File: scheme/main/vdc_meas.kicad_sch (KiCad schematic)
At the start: 22 parts, among them U12 AMC1311, U13 RS8551

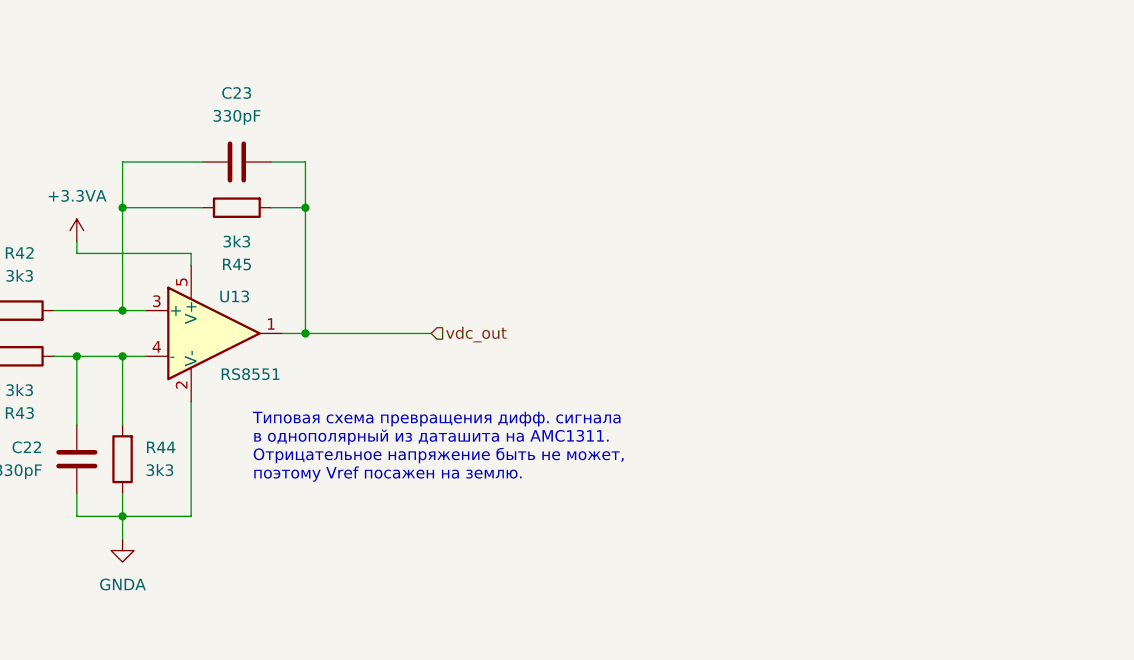
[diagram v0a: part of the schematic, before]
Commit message: added decoupling capacitors
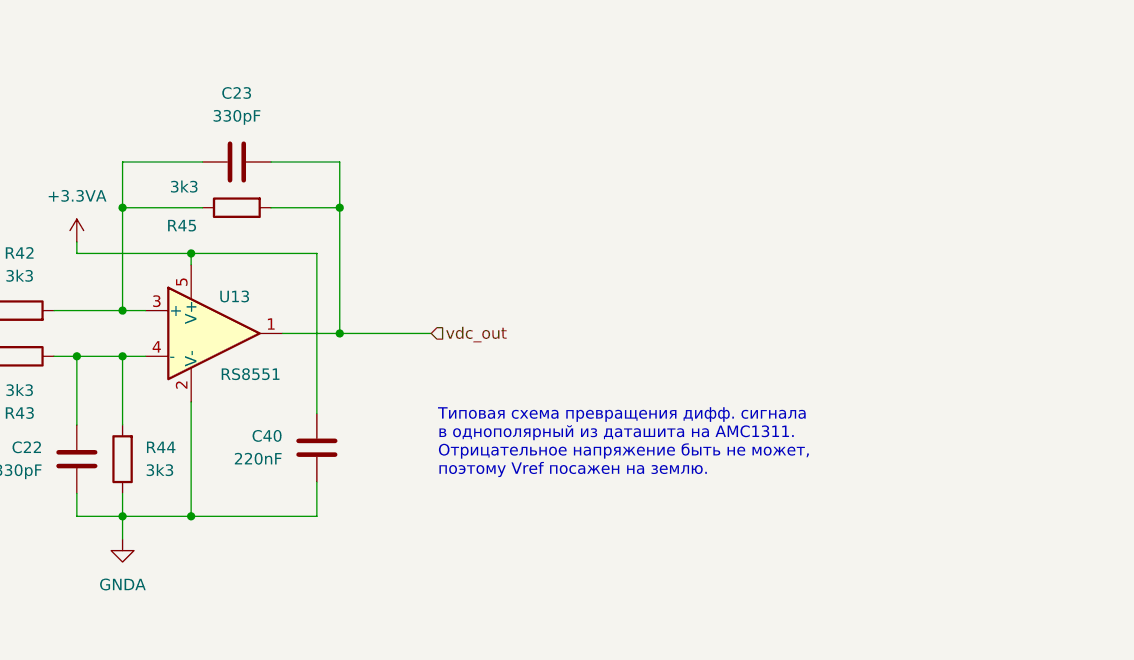
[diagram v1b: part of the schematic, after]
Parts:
- added C40: 220nF, Capacitor_SMD:C_0805_2012Metric, symbol Device:C
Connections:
- net +3.3VA: now also C40.1
- net GNDA: now also C40.2
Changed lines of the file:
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@@
+	)
+	(junction
+		(at 215.9 80.01)
+		(diameter 0)
+		(color 0 0 0 0)
 	)
 	(junction
@@
 	)
 	(junction
-		(at 212.09 80.01)
-		(diameter 0)
-		(color 0 0 0 0)
-	)
-	(junction
 		(at 186.69 82.55)
 		(diameter 0)
@@
 	)
 	(junction
+		(at 199.39 100.33)
+		(diameter 0)
+		(color 0 0 0 0)
+	)
+	(junction
 		(at 138.43 68.58)
 		(diameter 0)
@@
 	)
 	(junction
+		(at 199.39 71.12)
+		(diameter 0)
+		(color 0 0 0 0)
+	)
+	(junction
 		(at 191.77 66.04)
 		(diameter 0)
@@
 	)
 	(junction
+		(at 215.9 66.04)
+		(diameter 0)
+		(color 0 0 0 0)
+	)
+	(junction
 		(at 102.87 68.58)
 		(diameter 0)
@@
 		(color 0 0 0 0)
 	)
-	(junction
-		(at 212.09 66.04)
-		(diameter 0)
-		(color 0 0 0 0)
-	)
 	(wire
 		(pts
@@
 	(wire
 		(pts
-			(xy 212.09 66.04) (xy 212.09 80.01)
+			(xy 215.9 66.04) (xy 215.9 80.01)
 		)
 		(stroke
@@
 	(wire
 		(pts
+			(xy 213.36 71.12) (xy 199.39 71.12)
+		)
+		(stroke
+			(width 0)
+			(type default)
+		)
+	)
+	(wire
+		(pts
 			(xy 152.4 68.58) (xy 138.43 68.58)
 		)
@@
 	(wire
 		(pts
+			(xy 213.36 100.33) (xy 199.39 100.33)
+		)
+		(stroke
+			(width 0)
+			(type default)
+		)
+	)
+	(wire
+		(pts
 			(xy 191.77 66.04) (xy 191.77 77.47)
 		)
@@
 	(wire
 		(pts
-			(xy 208.28 66.04) (xy 212.09 66.04)
+			(xy 208.28 66.04) (xy 215.9 66.04)
 		)
 		(stroke
@@
 	(wire
 		(pts
+			(xy 213.36 88.9) (xy 213.36 71.12)
+		)
+		(stroke
+			(width 0)
+			(type default)
+		)
+	)
+	(wire
+		(pts
 			(xy 63.5 76.2) (xy 59.69 76.2)
 		)
@@
 	(wire
 		(pts
-			(xy 209.55 80.01) (xy 212.09 80.01)
+			(xy 209.55 80.01) (xy 215.9 80.01)
 		)
 		(stroke
@@
 	(wire
 		(pts
+			(xy 213.36 96.52) (xy 213.36 100.33)
+		)
+		(stroke
+			(width 0)
+			(type default)
+		)
+	)
+	(wire
+		(pts
 			(xy 184.15 77.47) (xy 191.77 77.47)
 		)
@@
 	(wire
 		(pts
+			(xy 215.9 80.01) (xy 226.06 80.01)
+		)
+		(stroke
+			(width 0)
+			(type default)
+		)
+	)
+	(wire
+		(pts
 			(xy 186.69 82.55) (xy 191.77 82.55)
 		)
@@
 	(wire
 		(pts
-			(xy 212.09 80.01) (xy 226.06 80.01)
-		)
-		(stroke
-			(width 0)
-			(type default)
-		)
-	)
-	(wire
-		(pts
 			(xy 133.35 67.31) (xy 133.35 68.58)
 		)
@@
 	(wire
 		(pts
-			(xy 208.28 60.96) (xy 212.09 60.96)
+			(xy 208.28 60.96) (xy 215.9 60.96)
 		)
 		(stroke
@@
 	(wire
 		(pts
-			(xy 212.09 60.96) (xy 212.09 66.04)
+			(xy 215.9 60.96) (xy 215.9 66.04)
 		)
 		(stroke
@@
 	(text "Типовая схема превращения дифф. сигнала\nв однополярный из даташита на AMC1311.\nОтрицательное напряжение быть не может,\nпоэтому Vref посажен на землю."
 		(exclude_from_sim no)
-		(at 206.248 92.71 0)
+		(at 226.822 92.202 0)
 		(effects
 			(font
@@
 		(dnp no)
 		(property "Reference" "R45"
-			(at 204.47 72.39 90)
+			(at 198.374 68.072 90)
 			(effects
 				(font
@@
 		)
 		(property "Value" "3k3"
-			(at 204.47 69.85 90)
+			(at 198.628 63.754 90)
 			(effects
 				(font
@@
 					(unit 1)
 				)
+			)
+		)
+	)
+	(symbol
+		(lib_id "Device:C")
+		(at 213.36 92.71 0)
+		(mirror y)
+		(unit 1)
+		(exclude_from_sim no)
+		(in_bom yes)
+		(on_board yes)
+		(dnp no)
+		(property "Reference" "C40"
+			(at 209.55 91.4399 0)
+			(effects
+				(font
+					(size 1.27 1.27)
+				)
+				(justify left)
+			)
+		)
+		(property "Value" "220nF"
+			(at 209.55 93.9799 0)
+			(effects
+				(font
+					(size 1.27 1.27)
+				)
+				(justify left)
+			)
+		)
+		(property "Footprint" "Capacitor_SMD:C_0805_2012Metric"
+			(at 212.3948 96.52 0)
+			(effects
+				(font
+					(size 1.27 1.27)
+				)
+				(hide yes)
+			)
+		)
+		(property "Datasheet" "~"
+			(at 213.36 92.71 0)
+			(effects
+				(font
+					(size 1.27 1.27)
+				)
+				(hide yes)
+			)
+		)
+		(property "Description" "Unpolarized capacitor"
+			(at 213.36 92.71 0)
+			(effects
+				(font
+					(size 1.27 1.27)
+				)
+				(hide yes)
+			)
+		)
+		(pin "2"
+		)
+		(pin "1"
+		)
+		(instances
+			(project "main"
+				(path "/c11d1dbc-4db9-4712-8d1d-5f6f7086cded/5d407613-ca47-4478-86ea-137e1786be86/ac75aa1d-a28e-4560-8180-07db9e006832"
+					(reference "C40")
+					(unit 1)
+				)

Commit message: bootstrap dc-dc add capacitors & more
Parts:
- renumbered C26 to C21, C27 to C22, C21 to C23, C29 to C26, C28 to C27, C22 to C28, C23 to C29, R51 to R40, R48 to R41, R49 to R42, R50 to R43, R52 to R44, R47 to R45, R40 to R47, R41 to R48, R42 to R49, R43 to R50, R44 to R51, R45 to R52

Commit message: separate hi power & signal gnd
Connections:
- net GNDPWR renamed GNDH
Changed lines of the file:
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@@
-	)
-	(symbol
-		(lib_id "power:GNDPWR")
-		(at 67.31 90.17 0)
-		(unit 1)
-		(exclude_from_sim no)
-		(in_bom yes)
-		(on_board yes)
-		(dnp no)
-		(property "Reference" "#PWR29"
-			(at 67.31 95.25 0)
-			(effects
-				(font
-					(size 1.27 1.27)
-				)
-				(hide yes)
-			)
-		)
-		(property "Value" "GNDPWR"
-			(at 67.183 93.98 0)
-			(effects
-				(font
-					(size 1.27 1.27)
-				)
-			)
-		)
-		(property "Footprint" ""
-			(at 67.31 91.44 0)
-			(effects
-				(font
-					(size 1.27 1.27)
-				)
-				(hide yes)
-			)
-		)
-		(property "Datasheet" ""
-			(at 67.31 91.44 0)
-			(effects
-				(font
-					(size 1.27 1.27)
-				)
-				(hide yes)
-			)
-		)
-		(property "Description" "Power symbol creates a global label with name \"GNDPWR\" , global ground"
-			(at 67.31 90.17 0)
-			(effects
-				(font
-					(size 1.27 1.27)
-				)
-				(hide yes)
-			)
-		)
-		(pin "1"
-		)
-		(instances
-			(project "main"
-				(path "/c11d1dbc-4db9-4712-8d1d-5f6f7086cded/65f1abf4-f16e-41b7-92a2-6e9eb3d99d97"
-					(reference "#PWR29")
-					(unit 1)
-				)
-			)
-		)
 	)
 	(symbol
@@
 	)
 	(symbol
-		(lib_id "power:GNDPWR")
-		(at 123.19 95.25 0)
-		(unit 1)
-		(exclude_from_sim no)
-		(in_bom yes)
-		(on_board yes)
-		(dnp no)
-		(property "Reference" "#PWR30"
-			(at 123.19 100.33 0)
-			(effects
-				(font
-					(size 1.27 1.27)
-				)
-				(hide yes)
-			)
-		)
-		(property "Value" "GNDPWR"
-			(at 123.063 99.06 0)
-			(effects
-				(font
-					(size 1.27 1.27)
-				)
-			)
-		)
-		(property "Footprint" ""
-			(at 123.19 96.52 0)
-			(effects
-				(font
-					(size 1.27 1.27)
-				)
-				(hide yes)
-			)
-		)
-		(property "Datasheet" ""
-			(at 123.19 96.52 0)
-			(effects
-				(font
-					(size 1.27 1.27)
-				)
-				(hide yes)
-			)
-		)
-		(property "Description" "Power symbol creates a global label with name \"GNDPWR\" , global ground"
-			(at 123.19 95.25 0)
-			(effects
-				(font
-					(size 1.27 1.27)
-				)
-				(hide yes)
-			)
-		)
-		(pin "1"
-		)
-		(instances
-			(project "main"
-				(path "/c11d1dbc-4db9-4712-8d1d-5f6f7086cded/65f1abf4-f16e-41b7-92a2-6e9eb3d99d97"
-					(reference "#PWR30")
-					(unit 1)
-				)
-			)
-		)
-	)
-	(symbol
 		(lib_id "Device:C")
 		(at 204.47 60.96 270)
@@
 					(unit 1)
 				)
+			)
+		)
+	)
+	(symbol
+		(lib_id "main:GNDH")
+		(at 67.31 90.17 0)
+		(unit 1)
+		(exclude_from_sim no)
+		(in_bom yes)
+		(on_board yes)
+		(dnp no)
+		(fields_autoplaced yes)
+		(property "Reference" "#PWR029"
+			(at 67.31 96.52 0)
+			(effects
+				(font
+					(size 1.27 1.27)
+				)
+				(hide yes)
+			)
+		)
+		(property "Value" "GNDH"
+			(at 67.31 95.25 0)
+			(effects
+				(font
+					(size 1.27 1.27)
+				)
+			)
+		)
+		(property "Footprint" ""
+			(at 67.31 90.17 0)
+			(effects
+				(font
+					(size 1.27 1.27)
+				)
+				(hide yes)
+			)
+		)
+		(property "Datasheet" ""
+			(at 67.31 90.17 0)
+			(effects
+				(font
+					(size 1.27 1.27)
+				)
+				(hide yes)
+			)
+		)
+		(property "Description" "Power symbol creates a global label with name \"GNDH\" , hi ground"
+			(at 67.31 90.17 0)
+			(effects
+				(font
+					(size 1.27 1.27)
+				)
+				(hide yes)
+			)
+		)
+		(pin "1"
+		)
+		(instances
+			(project "main"
+				(path "/c11d1dbc-4db9-4712-8d1d-5f6f7086cded/65f1abf4-f16e-41b7-92a2-6e9eb3d99d97"
+					(reference "#PWR029")
+					(unit 1)
+				)
+			)
+		)
+	)
+	(symbol
+		(lib_id "main:GNDH")
+		(at 123.19 95.25 0)
+		(unit 1)
+		(exclude_from_sim no)
+		(in_bom yes)
+		(on_board yes)
+		(dnp no)
+		(fields_autoplaced yes)
+		(property "Reference" "#PWR030"
+			(at 123.19 101.6 0)
+			(effects
+				(font
+					(size 1.27 1.27)
+				)
+				(hide yes)
+			)
+		)
+		(property "Value" "GNDH"
+			(at 123.19 100.33 0)
+			(effects
+				(font
+					(size 1.27 1.27)
+				)
+			)
+		)
+		(property "Footprint" ""
+			(at 123.19 95.25 0)
+			(effects
+				(font
+					(size 1.27 1.27)
+				)
+				(hide yes)
+			)
+		)
+		(property "Datasheet" ""
+			(at 123.19 95.25 0)
+			(effects
+				(font
+					(size 1.27 1.27)
+				)
+				(hide yes)
+			)
+		)
+		(property "Description" "Power symbol creates a global label with name \"GNDH\" , hi ground"
+			(at 123.19 95.25 0)
+			(effects
+				(font
+					(size 1.27 1.27)
+				)
+				(hide yes)
+			)
+		)
+		(pin "1"
+		)
+		(instances
+			(project "main"
+				(path "/c11d1dbc-4db9-4712-8d1d-5f6f7086cded/65f1abf4-f16e-41b7-92a2-6e9eb3d99d97"
+					(reference "#PWR030")
+					(unit 1)
+				)

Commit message: boards schematic sheets & more
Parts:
- added R107: 22R, Resistor_SMD:R_0805_2012Metric, symbol Device:R
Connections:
- net vdc_out: now also R107.2; no longer C29.1, R52.2, U13.1
- new net: C29.1, R107.1, R52.2, U13.1
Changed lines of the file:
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@@
+	)
+	(junction
+		(at 116.84 77.47)
+		(diameter 0)
+		(color 0 0 0 0)
+	)
+	(junction
+		(at 102.87 92.71)
+		(diameter 0)
+		(color 0 0 0 0)
+	)
+	(junction
+		(at 186.69 82.55)
+		(diameter 0)
+		(color 0 0 0 0)
+	)
+	(junction
+		(at 152.4 92.71)
+		(diameter 0)
+		(color 0 0 0 0)
+	)
+	(junction
+		(at 199.39 100.33)
+		(diameter 0)
+		(color 0 0 0 0)
+	)
+	(junction
+		(at 138.43 68.58)
+		(diameter 0)
+		(color 0 0 0 0)
+	)
+	(junction
+		(at 133.35 68.58)
+		(diameter 0)
+		(color 0 0 0 0)
+	)
+	(junction
+		(at 191.77 82.55)
+		(diameter 0)
+		(color 0 0 0 0)
+	)
+	(junction
+		(at 138.43 92.71)
+		(diameter 0)
+		(color 0 0 0 0)
+	)
+	(junction
+		(at 199.39 71.12)
+		(diameter 0)
+		(color 0 0 0 0)
+	)
+	(junction
+		(at 191.77 66.04)
+		(diameter 0)
+		(color 0 0 0 0)
+	)
+	(junction
+		(at 191.77 77.47)
+		(diameter 0)
+		(color 0 0 0 0)
+	)
+	(junction
+		(at 215.9 66.04)
+		(diameter 0)
+		(color 0 0 0 0)
+	)
+	(junction
+		(at 102.87 68.58)
+		(diameter 0)
+		(color 0 0 0 0)
 	)
 	(junction
@@
 	)
 	(junction
-		(at 116.84 77.47)
-		(diameter 0)
-		(color 0 0 0 0)
-	)
-	(junction
-		(at 102.87 92.71)
-		(diameter 0)
-		(color 0 0 0 0)
-	)
-	(junction
-		(at 186.69 82.55)
-		(diameter 0)
-		(color 0 0 0 0)
-	)
-	(junction
-		(at 152.4 92.71)
-		(diameter 0)
-		(color 0 0 0 0)
-	)
-	(junction
-		(at 199.39 100.33)
-		(diameter 0)
-		(color 0 0 0 0)
-	)
-	(junction
-		(at 138.43 68.58)
-		(diameter 0)
-		(color 0 0 0 0)
-	)
-	(junction
-		(at 133.35 68.58)
-		(diameter 0)
-		(color 0 0 0 0)
-	)
-	(junction
-		(at 191.77 82.55)
-		(diameter 0)
-		(color 0 0 0 0)
-	)
-	(junction
-		(at 138.43 92.71)
-		(diameter 0)
-		(color 0 0 0 0)
-	)
-	(junction
-		(at 199.39 71.12)
-		(diameter 0)
-		(color 0 0 0 0)
-	)
-	(junction
-		(at 191.77 66.04)
-		(diameter 0)
-		(color 0 0 0 0)
-	)
-	(junction
-		(at 191.77 77.47)
-		(diameter 0)
-		(color 0 0 0 0)
-	)
-	(junction
-		(at 215.9 66.04)
-		(diameter 0)
-		(color 0 0 0 0)
-	)
-	(junction
-		(at 102.87 68.58)
-		(diameter 0)
-		(color 0 0 0 0)
-	)
-	(junction
 		(at 116.84 92.71)
 		(diameter 0)
@@
 	(wire
 		(pts
+			(xy 215.9 80.01) (xy 219.71 80.01)
+		)
+		(stroke
+			(width 0)
+			(type default)
+		)
+	)
+	(wire
+		(pts
 			(xy 191.77 82.55) (xy 191.77 90.17)
 		)
@@
 	(wire
 		(pts
+			(xy 227.33 80.01) (xy 231.14 80.01)
+		)
+		(stroke
+			(width 0)
+			(type default)
+		)
+	)
+	(wire
+		(pts
 			(xy 63.5 36.83) (xy 67.31 36.83)
 		)
@@
 		(pts
 			(xy 165.1 92.71) (xy 152.4 92.71)
-		)
-		(stroke
-			(width 0)
-			(type default)
-		)
-	)
-	(wire
-		(pts
-			(xy 215.9 80.01) (xy 226.06 80.01)
 		)
 		(stroke
@@
 	(hierarchical_label "vdc_out"
 		(shape output)
-		(at 226.06 80.01 0)
+		(at 231.14 80.01 0)
 		(fields_autoplaced yes)
 		(effects
@@
 					(unit 1)
 				)
+			)
+		)
+	)
+	(symbol
+		(lib_id "Device:R")
+		(at 223.52 80.01 90)
+		(unit 1)
+		(exclude_from_sim no)
+		(in_bom yes)
+		(on_board yes)
+		(dnp no)
+		(fields_autoplaced yes)
+		(property "Reference" "R107"
+			(at 223.52 73.66 90)
+			(effects
+				(font
+					(size 1.27 1.27)
+				)
+			)
+		)
+		(property "Value" "22R"
+			(at 223.52 76.2 90)
+			(effects
+				(font
+					(size 1.27 1.27)
+				)
+			)
+		)
+		(property "Footprint" "Resistor_SMD:R_0805_2012Metric"
+			(at 223.52 81.788 90)
+			(effects
+				(font
+					(size 1.27 1.27)
+				)
+				(hide yes)
+			)
+		)
+		(property "Datasheet" "~"
+			(at 223.52 80.01 0)
+			(effects
+				(font
+					(size 1.27 1.27)
+				)
+				(hide yes)
+			)
+		)
+		(property "Description" "Resistor"
+			(at 223.52 80.01 0)
+			(effects
+				(font
+					(size 1.27 1.27)
+				)
+				(hide yes)
+			)
+		)
+		(pin "1"
+		)
+		(pin "2"
+		)
+		(instances
+			(project "main"
+				(path "/c11d1dbc-4db9-4712-8d1d-5f6f7086cded/65f1abf4-f16e-41b7-92a2-6e9eb3d99d97"
+					(reference "R107")
+					(unit 1)
+				)
